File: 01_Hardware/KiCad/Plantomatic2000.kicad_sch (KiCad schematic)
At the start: 200 parts, among them J101 Conn_02x05_Odd_Even, J102 Conn_02x03_Odd_Even, J103 USB_C_Receptacle_USB2.0_16P, J105 JST_B4B, J106 Line Select, J107 Manual Start, J108 Hour, J109 Minute, J110 JST_4B4, J111 System Reset, J112 JST_B2B, J113 JST_B2B, J114 System Wake Up, J115 Running LED, J116 JST_4B4, J117 Running LED, Q101 IRLL014NP, Q102 IRLL014NP, Q104 NVTA7002NT1G, Q105 RU1E002SPTCL, Q106 NVTA7002NT1G, Q107 NVTA7002NT1G, Q108 RU1E002SPTCL, Q109 NVTA7002NT1G, Q110 RU1E002SPTCL, Q111 DTC143Z, Q112 DTC143Z, Q113 CSD17313Q2, SW102 SW_Push, SW103 SW_Push, U101 XC6220B331MR, U102 nPM1300, U103 ESP32-WROOM-32E, U104 TPS61287, U105 USBLC6-2P6, U106 CP2102N-A02-GQFN24, U107 DS3231M, U108 AT24CS01-SSHM

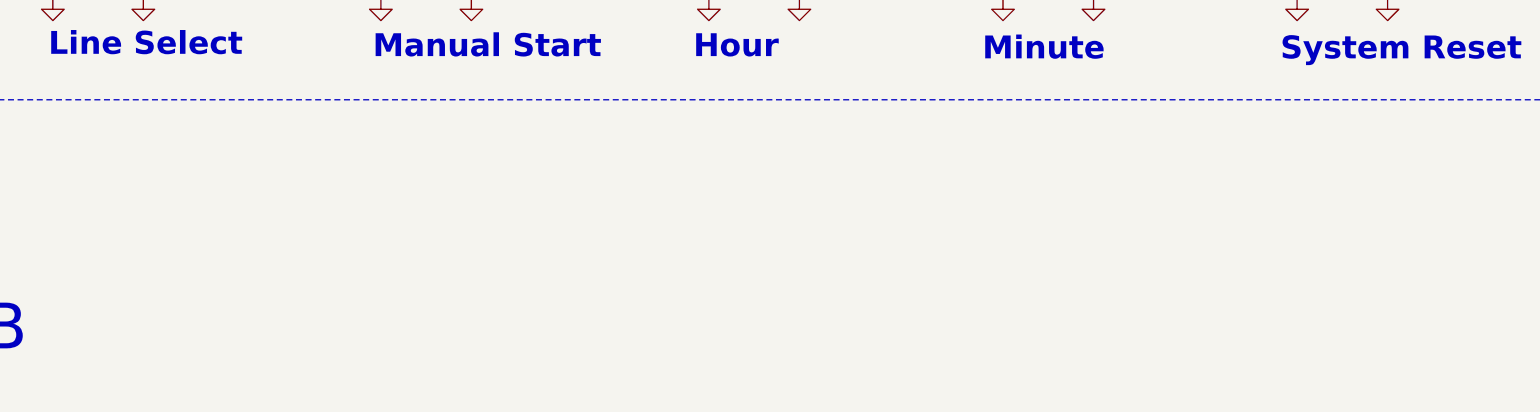
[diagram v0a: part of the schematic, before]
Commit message: PCB design continued -> Top layer mainly routed/ bottom layer GND pour and minor routing left to do + mounting holes
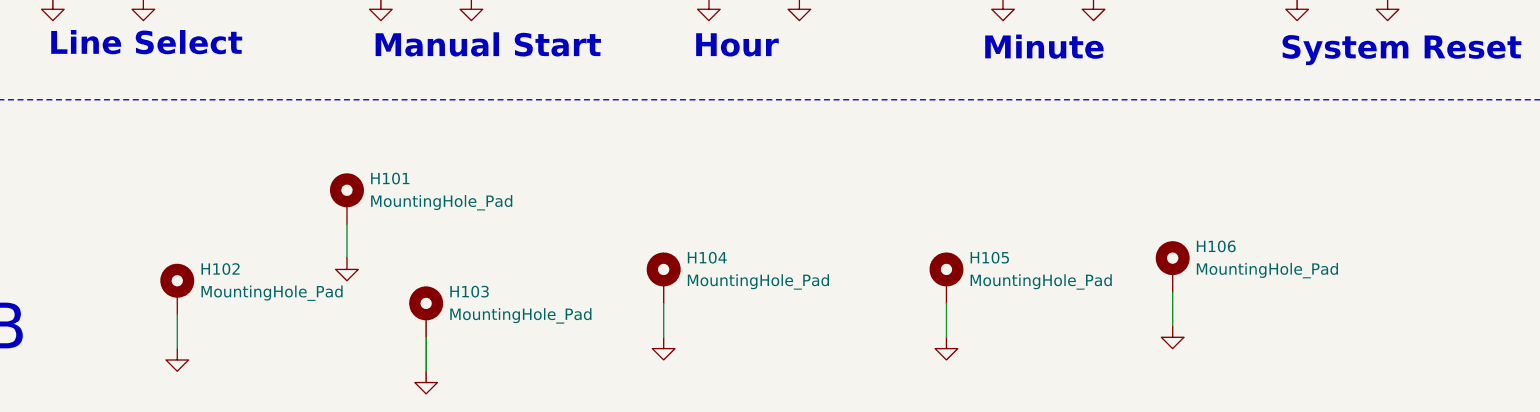
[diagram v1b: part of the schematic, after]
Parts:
- added H101, H102, H103, H104, H105, H106: MountingHole_Pad, MountingHole:MountingHole_2.2mm_M2_Pad_TopBottom, symbol Mechanical:MountingHole_Pad
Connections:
- net GND: now also H101.1, H102.1, H103.1, H104.1, H105.1, H106.1

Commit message: Finished PCB design
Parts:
- removed TP114, TP119, TP124, TP128, TP129: ~, TestPoint:TestPoint_Pad_D1.0mm, symbol Connector:TestPoint
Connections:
- net GND: now also J103.S1 (SHIELD)
- no-connect marks 25 -> 24

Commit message: Finished PCB design / Added Mounting holes position / Plantomatic2000.step generated / Gerber files generated
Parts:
- J117: value Running LED -> BATT
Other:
- note removed: "TO DO: BOM DESIGN PCB"
- moved on the sheet: H101, H102, H103, H104, H105, H106

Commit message: Added BOM / Slight adjustments to naming / Boost COUT 47uF not available in 0402 footprint -> ordered 1206 and 22uF 0805 as bacukp
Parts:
- C121: footprint Capacitor_SMD:C_0603_1608Metric -> Capacitor_SMD:C_1206_3216Metric
- D103, D104: value SML-P13PTT86R -> SML-P12U2TT86R
- D108, D109, D110: value SS14 -> SS14M
- J106: value Line Select -> JST_B2B
- J107: value Manual Start -> JST_B2B
- J108: value Hour -> JST_B2B
- J109: value Minute -> JST_B2B
- J110, J116: value JST_4B4 -> JST_B4B
- J111: value System Reset -> JST_B2B
- J114: value System Wake Up -> JST_B2B
- J115: value Running LED -> JST_B2B
- J117: value BATT -> JST_B2B
- Q101, Q102: value IRLL014NP -> STN3NF06L
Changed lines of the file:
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@@
 			)
 		)
-		(property "Value" "Line Select"
+		(property "Value" "JST_B2B"
 			(at 81.788 312.42 0)
 			(effects
@@
 			)
 		)
-		(property "Value" "SML-P13PTT86R"
+		(property "Value" "SML-P12U2TT86R"
 			(at 215.392 257.048 0)
 			(effects
@@
 			)
 		)
-		(property "Value" "SS14"
+		(property "Value" "SS14M"
 			(at 443.484 76.2 90)
 			(effects
@@
 			)
 		)
-		(property "Value" "BATT"
-			(at 229.616 52.07 0)
+		(property "Value" "JST_B2B"
+			(at 228.092 52.07 0)
 			(effects
 				(font
@@
 			)
 		)
-		(property "Footprint" "Capacitor_SMD:C_0603_1608Metric"
+		(property "Footprint" "Capacitor_SMD:C_1206_3216Metric"
 			(at 435.61 161.29 0)
 			(effects
@@
 			)
 		)
-		(property "Value" "Minute"
+		(property "Value" "JST_B2B"
 			(at 188.468 312.42 0)
 			(effects
@@
 			)
 		)
-		(property "Value" "JST_4B4"
+		(property "Value" "JST_B4B"
 			(at 218.186 81.28 0)
 			(effects
@@
 			)
 		)
-		(property "Value" "IRLL014NP"
+		(property "Value" "STN3NF06L"
 			(at 464.82 41.9099 0)
 			(effects
@@
 			)
 		)
-		(property "Value" "Manual Start"
+		(property "Value" "JST_B2B"
 			(at 118.618 312.42 0)
 			(effects
@@
 		(dnp no)
 		(property "Reference" "R116"
-			(at 71.628 225.044 90)
+			(at 70.866 225.298 90)
 			(effects
 				(font
@@
 			)
 		)
-		(property "Value" "System Reset"
-			(at 228.092 312.42 0)
+		(property "Value" "JST_B2B"
+			(at 225.298 312.42 0)
 			(effects
 				(font
@@
 			)
 		)
-		(property "Value" "JST_4B4"
+		(property "Value" "JST_B4B"
 			(at 547.624 229.87 0)
 			(effects
@@
 		(dnp no)
 		(property "Reference" "D110"
-			(at 72.644 219.71 0)
+			(at 71.12 220.218 0)
 			(effects
 				(font
@@
 			)
 		)
-		(property "Value" "SS14"
-			(at 78.994 219.964 0)
+		(property "Value" "SS14M"
+			(at 78.232 219.964 0)
 			(effects
 				(font
@@
 			)
 		)
-		(property "Value" "IRLL014NP"
+		(property "Value" "STN3NF06L"
 			(at 464.82 90.1699 0)
 			(effects
@@
 			)
 		)
-		(property "Value" "System Wake Up"
+		(property "Value" "JST_B2B"
 			(at 42.418 312.42 0)
 			(effects
@@
 			)
 		)
-		(property "Value" "Running LED"
-			(at 262.382 313.69 0)
+		(property "Value" "JST_B2B"
+			(at 259.588 313.69 0)
 			(effects
 				(font
@@
 			)
 		)
-		(property "Value" "SML-P13PTT86R"
+		(property "Value" "SML-P12U2TT86R"
 			(at 215.392 259.08 0)
 			(effects
@@
 			)
 		)
-		(property "Value" "Hour"
+		(property "Value" "JST_B2B"
 			(at 155.448 312.42 0)
 			(effects
@@
 			)
 		)
-		(property "Value" "SS14"
+		(property "Value" "SS14M"
 			(at 443.484 27.94 90)
 			(effects
